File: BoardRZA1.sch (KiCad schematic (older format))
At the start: 183 parts, among them CON1 USB-MINI-B, CON2 USB-A-PCB, CON3 microSD, CON4 BARREL_JACK, J1 HR911105A, J2 SIL38, K1 CONN_3, P1 CONN_5X2, P10 CONN_1, P11 CONN_1, P12 CONN_1, P13 CONN_1, P14 CONN_1, P15 CONN_1, P16 CONN_1, P17 CONN_1, P2 CONN_1, P3 CONN_1, P4 CONN_1, P5 CONN_1, P6 CONN_1, P7 CONN_1, P8 CONN_1, P9 CONN_1, SW1 RESET, SW2 NMI, SW3 SW0, SW4 SW1, U1 RZ-A1L, U2 13MHz, U3 48MHz, U4 N25QXXX, U5 AS4C16M16S, U6 BA3259HFP, U7 BU42xx, U8 KSZ8041MLL, U9 25MHz, X1 32.768k

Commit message: Added VGA out, remove eth
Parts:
- removed C54, C63: 22u, footprints:SM0805, symbol Csmall
- removed C55, C56, C57, C59, C60, C61, C62, C64, C65, C66: 100n, footprints:SM0805, symbol Csmall
- removed C58: 100p, footprints:SM0805, symbol Csmall
- removed J1: HR911105A, footprints:RJ45_Pulse_J403-A, symbol HR911105A
- removed L10: BLM18PG600, footprints:SM0805, symbol INDUCTOR_SMALL
- removed R27, R28, R29, R30, R31, R32: 33R, footprints:SM0805, symbol R
- removed R33, R34, R35: 4K7, footprints:SM0805, symbol R
- removed R36, R37, R49: 220R, footprints:SM0805, symbol R
- removed R38, R39, R40, R41: 49.9, footprints:SM0805, symbol R
- removed U8: KSZ8041MLL, footprints:LQFP48-M05, symbol KSZ8041MLL
- removed U9: 25MHz, footprints:OSC_4PIN, symbol OSC_4PIN
- added J1: VGA, footprints:DB_15F-VGA, symbol VGA
- added RP1, RP2, RP3: 20k, Resistors_SMD:r_cat16-8, symbol R_PACK8
- added RP4, RP5, RP6: 10k, Resistors_SMD:r_cat16-8, symbol R_PACK8
- added U8: TL074, SMD_Packages:SO14E, symbol TL074
- R21: value 6.49k -> 10k
- R22: value 4K7 -> 10k
- R23: value 33R -> 10k
- R24, R25, R26: value 33R -> 280R
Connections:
- net ET_MDC is gone; now on net LED2: U1.72 (P9_0/ET_MDC/SD_D1_0/TxD1)
- net ET_MDIO is gone; now on net LED3: U1.73 (P9_1/ET_MDIO/SD_D0_0/CTS0)
- net PHY_RESET is gone; now on net SW1: U1.189 (P4_1/A18/VIO_HD/TIOC2B/ET_MDIO/RTS1)
- net +3.3V: now also U8.4 (V+); no longer R22.1
- net LED0: now also U1.70 (P8_14/LCD0_TCON6/ET_COL/SD_CD_0/SCK1); no longer U1.17 (P6_0/D16/LCD0_DATA8/RSPCK0/TCLKA/WDTOVF)
- net LED1: now also U1.71 (P8_15/ET_CRS/SD_WP_0/RxD1); no longer U1.19 (P6_1/D17/LCD0_DATA9/SSL00/TCLKB)
- net LED2: no longer U1.20 (P6_2/D18/LCD0_DATA10/MOSI0/TCLKC)
- net LED3: no longer U1.22 (P6_3/D19/LCD0_DATA11/MISO0/TCLKD)
- net P1_10: now also J2.23; no longer J2.19
- net P1_11: now also J2.22; no longer J2.18
- net P1_12: now also J2.21; no longer J2.17
- net P1_13: now also J2.20; no longer J2.16
- net P1_14: now also J2.19; no longer J2.15
- net P1_15: now also J2.18; no longer J2.14
- net P1_8: now also J2.25; no longer J2.21
- net P1_9: now also J2.24; no longer J2.20
- net P7_10: now also J2.29; no longer J2.25
- net P7_11: now also J2.28; no longer J2.24
- net P7_8: now also J2.31; no longer J2.27
- net P7_9: now also J2.30; no longer J2.26
- net P8_12: now also J2.27; no longer J2.23
- net P8_13: now also J2.26; no longer J2.22
- net SW0: now also U1.188 (P4_0/A17/VIO_VD/TIOC1B/ET_MDC/CTS1); no longer U1.26 (P6_5/D21/LCD0_DATA13/SSIWS3/MLB_SIG)
- net SW1: no longer U1.24 (P6_4/D20/LCD0_DATA12/SSISCK3/MLB_CLK)
- net VSS: now also R22.1, R23.1, J1.10 (GND_VSYNC), J1.5 (GND_HSYNC), J1.6 (RED_RTN), J1.7 (GREEN_RTN), J1.8 (BLUE_RTN), J1.9 (KEY/PWR), U8.11 (V-)
- net P9_5: now reaches U1.137 (P9_5/MISO2/SD_D2_0/TxD0/TIOC2B)
- net P9_5: now also J2.14
- net at R21.2: now also RP4.9 (R8)
- net at R26.2: now also J1.1 (RED)
- net at R22.2: now also RP5.9 (R8)
- net at R25.2: now also J1.2 (GREEN)
- net at R24.2: now also J1.3 (BLUE)
- net at R23.2: now also RP6.9 (R8)
- net ET_COL: no longer names the net of R24.1
- net ET_COL: now also U8.1, U8.2 (-); no longer U1.70 (P8_14/LCD0_TCON6/ET_COL/SD_CD_0/SCK1)
- removed net ET_CRS: R23.1, U1.71 (P8_15/ET_CRS/SD_WP_0/RxD1)
- net ET_RXCLK: no longer names the net of R26.1
- net ET_RXCLK: now also U8.8, U8.9 (-); no longer U1.127 (P9_2/RSPCK2/ET_RXCLK/SD_CLK_0/RTS0/TIOC1A)
- net ET_RXD0 renamed LCD_DATA7
- net LCD_DATA7: now also RP3.1 (P1)
- net ET_RXD1 renamed LCD_HSYNC
- net LCD_HSYNC: now also J1.13 (HSYNC)
- net ET_RXD2 renamed LCD_VSYNC
- net LCD_VSYNC: now also J1.14 (VSYNC)
- net ET_RXD3 renamed LCD_PCLK
- net ET_RXDV renamed P9_4
- net P9_4: now also J2.15
- net ET_RXER renamed P9_3
- net P9_3: now also J2.16
- net ET_TXCLK: no longer names the net of R25.1
- net ET_TXCLK: now also U8.6 (-), U8.7; no longer U1.200 (P8_4/LCD0_DATA4/ET_TXCLK/CTS2/TIOC0A)
- net ET_TXD0 renamed LCD_DATA0
- net LCD_DATA0: now also RP3.8 (P8)
- net ET_TXD1 renamed LCD_DATA1
- net LCD_DATA1: now also RP3.7 (P7)
- net ET_TXD2 renamed LCD_DATA2
- net LCD_DATA2: now also RP3.6 (P6)
- net ET_TXD3 renamed LCD_DATA3
- net LCD_DATA3: now also RP3.5 (P5)
- net ET_TXEN renamed LCD_DATA6
- net LCD_DATA6: now also RP3.2 (P2)
- net P6_10: no longer names the net of J2.33
- net P6_10: no longer U1.40 (P6_10/D26/LCD0_DATA18/SSITxD0/IRQ3/TIOC3D/CAN1_TX)
- net P6_11: no longer names the net of J2.32
- net P6_11: no longer U1.41 (P6_11/D27/LCD0_DATA19/SSIRxD0/SSI_DATA2/SCK0/CAN1_RX)
- net P6_12 renamed LCD_DATA20
- net LCD_DATA20: now also RP1.4 (P4); no longer J2.31
- net P6_13 renamed LCD_DATA21
- net LCD_DATA21: now also RP1.3 (P3); no longer J2.30
- net P6_14 renamed LCD_DATA22
- net LCD_DATA22: now also RP1.2 (P2); no longer J2.29
- net P6_15 renamed LCD_DATA23
- net LCD_DATA23: now also RP1.1 (P1); no longer J2.28
- net P6_6: no longer names the net of J2.37
- net P6_6: no longer U1.31 (P6_6/D22/LCD0_DATA14/SSITxD3/MLB_DAT)
- net P6_7: no longer names the net of J2.36
- net P6_7: no longer U1.32 (P6_7/D23/LCD0_DATA15/SSIRxD3/IRQ0/TIOC3A/RLIN30/RX)
- net P6_8: no longer names the net of J2.35
- net P6_8: no longer U1.33 (P6_8/D24/LCD0_DATA16/SSISCK0/IRQ1/TIOC3B/RLIN30/TX)
- net P6_9: no longer names the net of J2.34
- net P6_9: no longer U1.38 (P6_9/D25/LCD0_DATA17/SSIWS0/IRQ2/TIOC3C)
- net P8_11: no longer names the net of U1.37 (P8_11/LCD0_TCON3/SSISCK2/SCK4)
- net TX_TXER renamed LCD_DATA5
- net LCD_DATA5: now also RP3.3 (P3)
- new net: RP3.9 (R8), RP6.10 (R7), RP6.8 (P8)
- new net: RP3.10 (R7), RP6.11 (R6), RP6.7 (P7)
- new net: RP3.11 (R6), RP6.12 (R5), RP6.6 (P6)
- new net: RP3.12 (R5), RP6.13 (R4), RP6.5 (P5)
- new net: RP3.13 (R4), RP6.14 (R3), RP6.4 (P4)
- new net: RP3.14 (R3), RP6.15 (R2), RP6.3 (P3)
- new net: RP3.15 (R2), RP6.16 (R1), RP6.2 (P2)
- new net: RP2.9 (R8), RP5.10 (R7), RP5.8 (P8)
- new net: RP2.10 (R7), RP5.11 (R6), RP5.7 (P7)
- new net: RP2.11 (R6), RP5.12 (R5), RP5.6 (P6)
- new net: RP2.12 (R5), RP5.13 (R4), RP5.5 (P5)
- new net: RP2.13 (R4), RP5.14 (R3), RP5.4 (P4)
- new net: RP2.14 (R3), RP5.15 (R2), RP5.3 (P3)
- new net: RP2.15 (R2), RP5.16 (R1), RP5.2 (P2)
- new net: RP1.9 (R8), RP4.10 (R7), RP4.8 (P8)
- new net: RP1.10 (R7), RP4.11 (R6), RP4.7 (P7)
- new net: RP1.11 (R6), RP4.12 (R5), RP4.6 (P6)
- new net: RP1.12 (R5), RP4.13 (R4), RP4.5 (P5)
- new net: RP1.13 (R4), RP4.14 (R3), RP4.4 (P4)
- new net: RP1.14 (R3), RP4.15 (R2), RP4.3 (P3)
- new net: RP1.15 (R2), RP4.16 (R1), RP4.2 (P2)
- new net LCD_DATA10: RP2.6 (P6), U1.20 (P6_2/D18/LCD0_DATA10/MOSI0/TCLKC)
- new net LCD_DATA11: RP2.5 (P5), U1.22 (P6_3/D19/LCD0_DATA11/MISO0/TCLKD)
- new net LCD_DATA12: RP2.4 (P4), U1.24 (P6_4/D20/LCD0_DATA12/SSISCK3/MLB_CLK)
- new net LCD_DATA13: RP2.3 (P3), U1.26 (P6_5/D21/LCD0_DATA13/SSIWS3/MLB_SIG)
- new net LCD_DATA14: RP2.2 (P2), U1.31 (P6_6/D22/LCD0_DATA14/SSITxD3/MLB_DAT)
- new net LCD_DATA15: RP2.1 (P1), U1.32 (P6_7/D23/LCD0_DATA15/SSIRxD3/IRQ0/TIOC3A/RLIN30/RX)
- new net LCD_DATA16: RP1.8 (P8), U1.33 (P6_8/D24/LCD0_DATA16/SSISCK0/IRQ1/TIOC3B/RLIN30/TX)
- new net LCD_DATA17: RP1.7 (P7), U1.38 (P6_9/D25/LCD0_DATA17/SSIWS0/IRQ2/TIOC3C)
- new net LCD_DATA18: RP1.6 (P6), U1.40 (P6_10/D26/LCD0_DATA18/SSITxD0/IRQ3/TIOC3D/CAN1_TX)
- new net LCD_DATA19: RP1.5 (P5), U1.41 (P6_11/D27/LCD0_DATA19/SSIRxD0/SSI_DATA2/SCK0/CAN1_RX)
- new net LCD_DATA4: RP3.4 (P4), U1.200 (P8_4/LCD0_DATA4/ET_TXCLK/CTS2/TIOC0A)
- new net LCD_DATA8: RP2.8 (P8), U1.17 (P6_0/D16/LCD0_DATA8/RSPCK0/TCLKA/WDTOVF)
- new net LCD_DATA9: RP2.7 (P7), U1.19 (P6_1/D17/LCD0_DATA9/SSL00/TCLKB)
- new net P9_2: J2.17, U1.127 (P9_2/RSPCK2/ET_RXCLK/SD_CLK_0/RTS0/TIOC1A)
- new net VGA_B: RP1.16 (R1), RP4.1 (P1), U8.3 (+)
- new net VGA_G: RP2.16 (R1), RP5.1 (P1), U8.5 (+)
- new net VGA_R: RP3.16 (R1), RP6.1 (P1), U8.10 (+)
- no-connect marks 17 -> 14
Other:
- note removed: "LED0: PU\nLED1: PD"

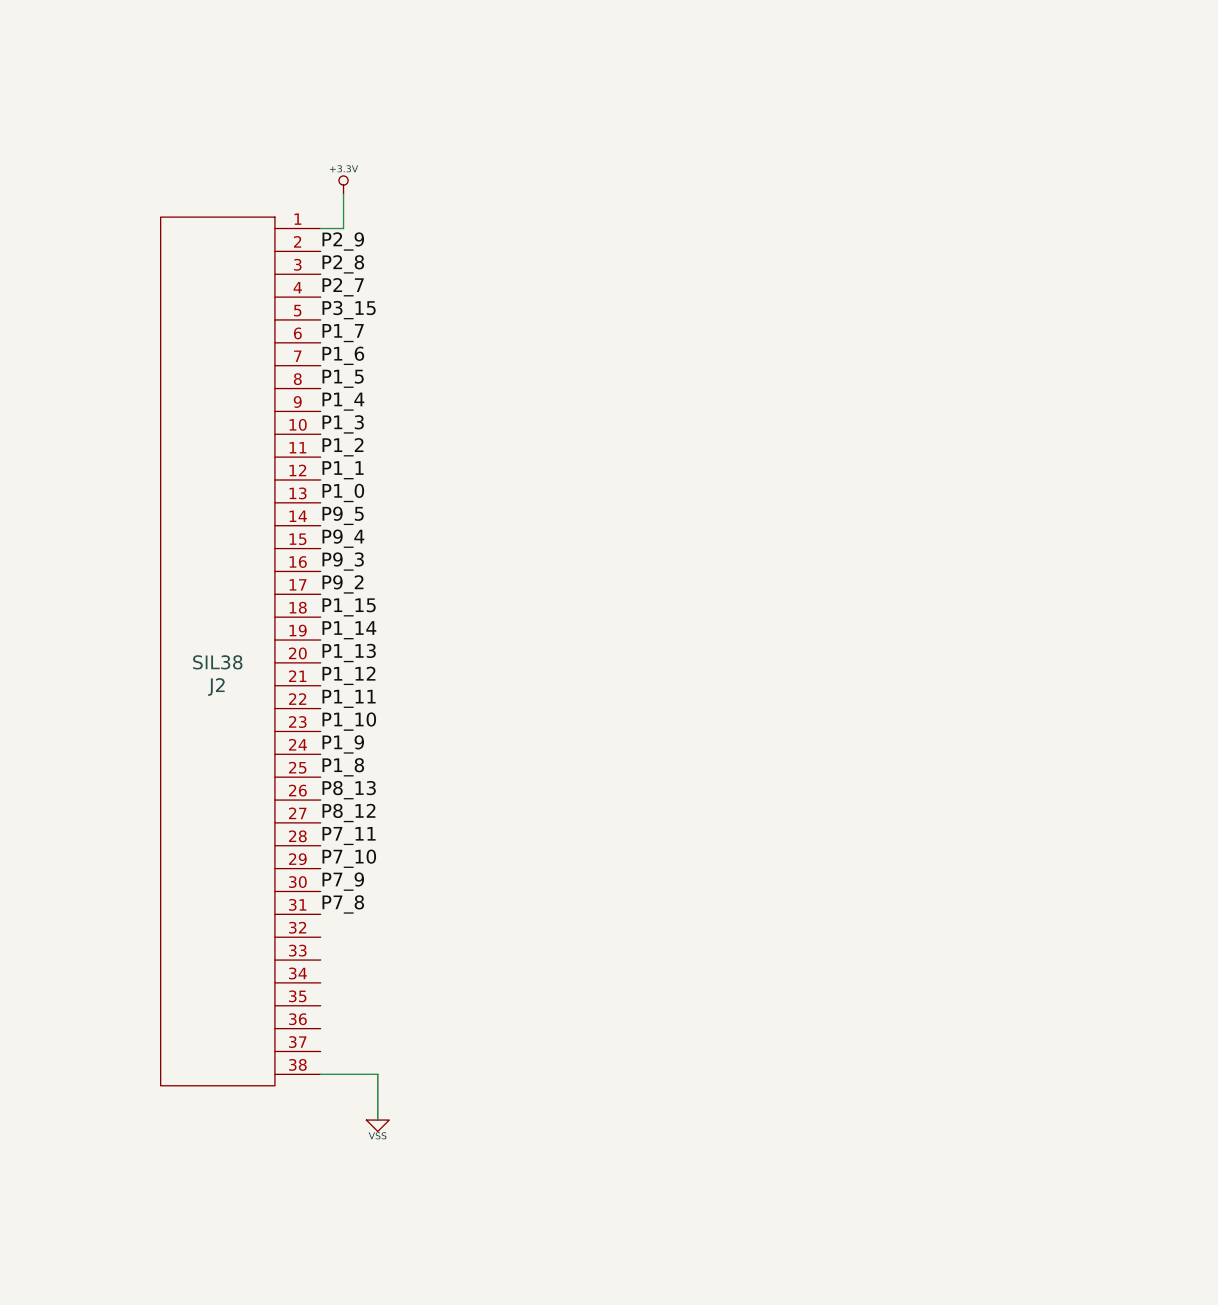
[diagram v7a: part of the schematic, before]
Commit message: Resize board, move VGA connector and R2R DAC
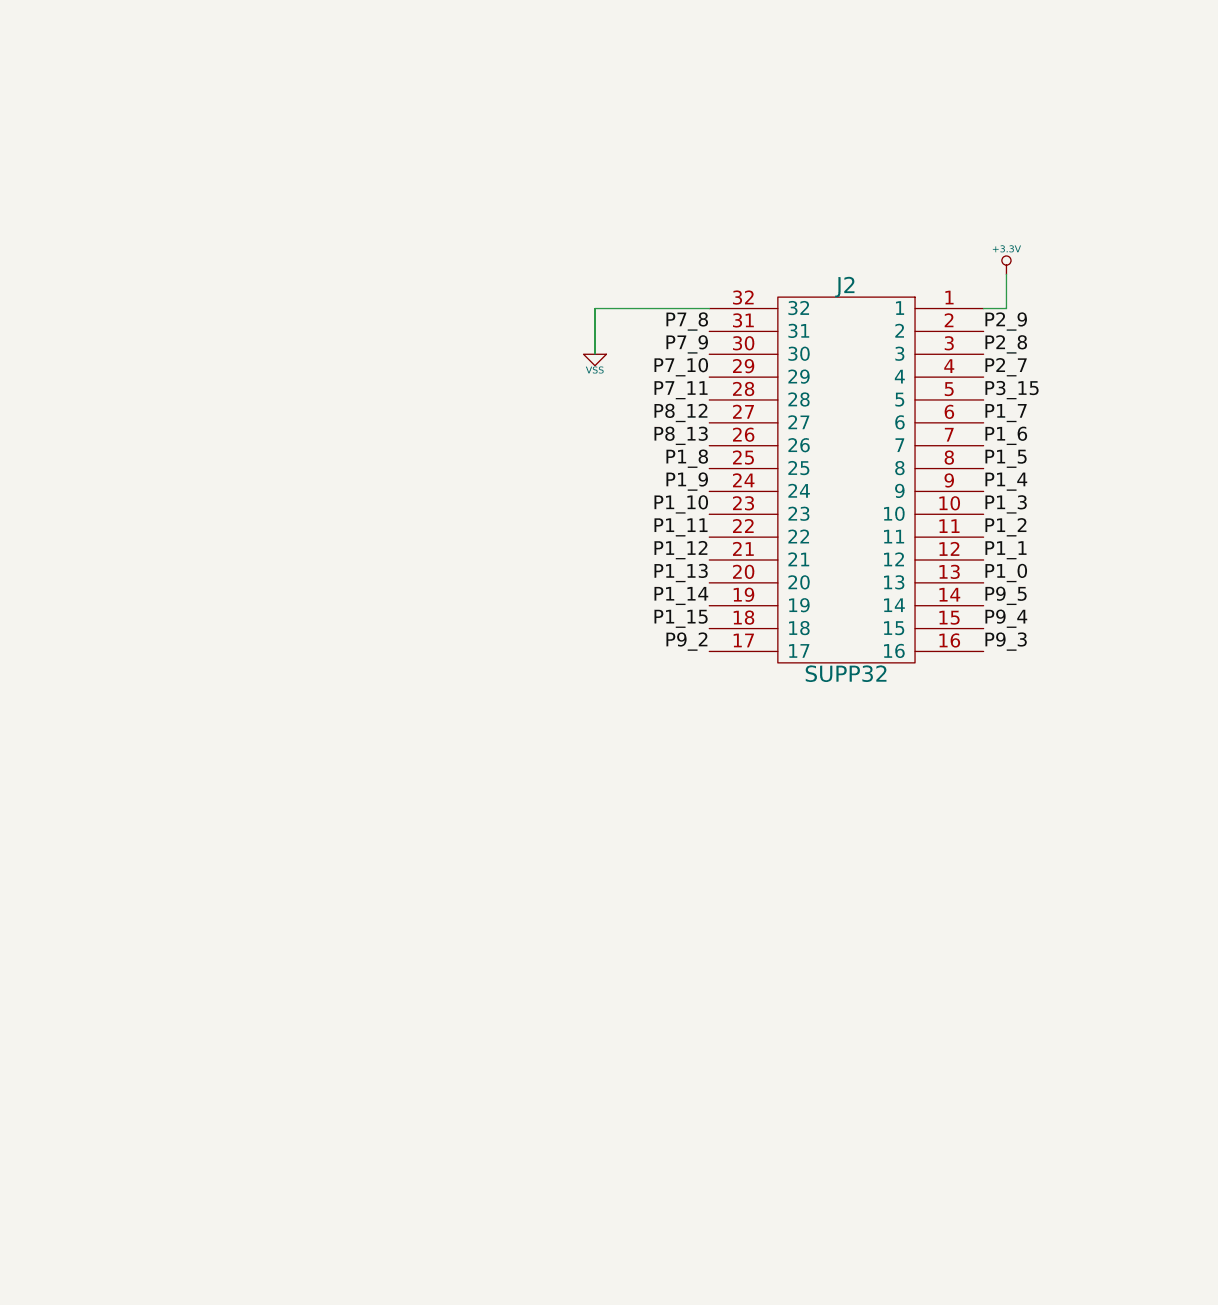
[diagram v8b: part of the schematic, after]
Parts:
- removed J2: SIL38, footprints:Pin_Header_Angled_1x38, symbol SIL38
- added J2: SUPP32, Pin_Headers:Pin_Header_Angled_1x32, symbol SUPP32
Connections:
- net +3.3V: now also J2.1
- net P1_0: now also J2.13
- net P1_1: now also J2.12
- net P1_10: now also J2.23
- net P1_11: now also J2.22
- net P1_12: now also J2.21
- net P1_13: now also J2.20
- net P1_14: now also J2.19
- net P1_15: now also J2.18
- net P1_2: now also J2.11
- net P1_3: now also J2.10
- net P1_4: now also J2.9
- net P1_5: now also J2.8
- net P1_6: now also J2.7
- net P1_7: now also J2.6
- net P1_8: now also J2.25
- net P1_9: now also J2.24
- net P2_7: now also J2.4
- net P2_8: now also J2.3
- net P2_9: now also J2.2
- net P3_15: now also J2.5
- net P7_10: now also J2.29
- net P7_11: now also J2.28
- net P7_8: now also J2.31
- net P7_9: now also J2.30
- net P8_12: now also J2.27
- net P8_13: now also J2.26
- net P9_2: now also J2.17
- net P9_3: now also J2.16
- net P9_4: now also J2.15
- net P9_5: now also J2.14
- net VSS: now also J2.32
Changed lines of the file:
@@
 L VSS #PWR048
 U 1 1 546806AB
-P 8350 12150
-F 0 "#PWR048" H 8350 12150 30  0001 C CNN
-F 1 "VSS" H 8350 12080 30  0000 C CNN
-F 2 "" H 8350 12150 60  0000 C CNN
-F 3 "" H 8350 12150 60  0000 C CNN
-	1    8350 12150
-	1    0    0    -1
+P 9300 8800
+F 0 "#PWR048" H 9300 8800 30  0001 C CNN
+F 1 "VSS" H 9300 8730 30  0000 C CNN
+F 2 "" H 9300 8800 60  0000 C CNN
+F 3 "" H 9300 8800 60  0000 C CNN
+	1    9300 8800
+	-1   0    0    -1
 $EndComp
 $Comp
 L +3.3V #PWR049
 U 1 1 54681794
-P 8200 8100
-F 0 "#PWR049" H 8200 8060 30  0001 C CNN
-F 1 "+3.3V" H 8200 8210 30  0000 C CNN
-F 2 "" H 8200 8100 60  0000 C CNN
-F 3 "" H 8200 8100 60  0000 C CNN
-	1    8200 8100
-	1    0    0    -1
-$EndComp
-$Comp
-L SIL38 J2
-U 1 1 5468523A
-P 7650 10200
-F 0 "J2" H 7650 10150 60  0000 C CNN
-F 1 "SIL38" H 7650 10250 60  0000 C CNN
-F 2 "footprints:Pin_Header_Angled_1x38" H 7650 10200 60  0001 C CNN
-F 3 "" H 7650 10200 60  0000 C CNN
-	1    7650 10200
-	-1   0    0    -1
+P 11100 8450
+F 0 "#PWR049" H 11100 8410 30  0001 C CNN
+F 1 "+3.3V" H 11100 8560 30  0000 C CNN
+F 2 "" H 11100 8450 60  0000 C CNN
+F 3 "" H 11100 8450 60  0000 C CNN
+	1    11100 8450
+	1    0    0    -1
 $EndComp
 Text Label 27950 13350 0    60   ~ 0
@@
 Text Label 27950 12650 0    60   ~ 0
 P1_7
-Text Label 8100 9450 0    60   ~ 0
+Text Label 11000 9800 0    60   ~ 0
 P1_0
-Text Label 8100 9350 0    60   ~ 0
+Text Label 11000 9700 0    60   ~ 0
 P1_1
-Text Label 8100 9250 0    60   ~ 0
+Text Label 11000 9600 0    60   ~ 0
 P1_2
-Text Label 8100 9150 0    60   ~ 0
+Text Label 11000 9500 0    60   ~ 0
 P1_3
-Text Label 8100 9050 0    60   ~ 0
+Text Label 11000 9400 0    60   ~ 0
 P1_4
-Text Label 8100 8950 0    60   ~ 0
+Text Label 11000 9300 0    60   ~ 0
 P1_5
-Text Label 8100 8850 0    60   ~ 0
+Text Label 11000 9200 0    60   ~ 0
 P1_6
-Text Label 8100 8750 0    60   ~ 0
+Text Label 11000 9100 0    60   ~ 0
 P1_7
 Text Label 27950 12550 0    60   ~ 0
@@
 P2_9
 NoConn ~ 27950 11850
-Text Label 8100 8550 0    60   ~ 0
+Text Label 11000 8900 0    60   ~ 0
 P2_7
-Text Label 8100 8450 0    60   ~ 0
+Text Label 11000 8800 0    60   ~ 0
 P2_8
-Text Label 8100 8350 0    60   ~ 0
+Text Label 11000 8700 0    60   ~ 0
 P2_9
-Text Label 8100 8650 0    60   ~ 0
+Text Label 11000 9000 0    60   ~ 0
 P3_15
 Text Label 18650 17450 2    60   ~ 0
@@
 Text Label 18650 16750 2    60   ~ 0
 P1_8
-Text Label 8100 9950 0    60   ~ 0
+Text Label 9800 10000 2    60   ~ 0
 P1_15
-Text Label 8100 10050 0    60   ~ 0
+Text Label 9800 9900 2    60   ~ 0
 P1_14
-Text Label 8100 10150 0    60   ~ 0
+Text Label 9800 9800 2    60   ~ 0
 P1_13
-Text Label 8100 10250 0    60   ~ 0
+Text Label 9800 9700 2    60   ~ 0
 P1_12
-Text Label 8100 10350 0    60   ~ 0
+Text Label 9800 9600 2    60   ~ 0
 P1_11
-Text Label 8100 10450 0    60   ~ 0
+Text Label 9800 9500 2    60   ~ 0
 P1_10
-Text Label 8100 10550 0    60   ~ 0
+Text Label 9800 9400 2    60   ~ 0
 P1_9
-Text Label 8100 10650 0    60   ~ 0
+Text Label 9800 9300 2    60   ~ 0
 P1_8
 $Comp
@@
 Text Label 18650 14550 2    60   ~ 0
 P8_13
-Text Label 8100 11250 0    60   ~ 0
+Text Label 9800 8700 2    60   ~ 0
 P7_8
-Text Label 8100 11150 0    60   ~ 0
+Text Label 9800 8800 2    60   ~ 0
 P7_9
-Text Label 8100 11050 0    60   ~ 0
+Text Label 9800 8900 2    60   ~ 0
 P7_10
-Text Label 8100 10950 0    60   ~ 0
+Text Label 9800 9000 2    60   ~ 0
 P7_11
 Text Label 18650 14850 2    60   ~ 0
@@
 Text Label 28000 17450 0    60   ~ 0
 MD_BOOT0
-Text Label 8100 10850 0    60   ~ 0
+Text Label 9800 9100 2    60   ~ 0
 P8_12
-Text Label 8100 10750 0    60   ~ 0
+Text Label 9800 9200 2    60   ~ 0
 P8_13
 Text Label 16700 14050 2    60   ~ 0
@@
 Connection ~ 16800 3900
 Wire Wire Line
-	8350 12150 8350 11950
-Wire Wire Line
-	8350 11950 8100 11950
-Wire Wire Line
-	8200 8100 8200 8250
-Wire Wire Line
-	8200 8250 8100 8250
+	9300 8800 9300 8600
+Wire Wire Line
+	9300 8600 9800 8600
+Wire Wire Line
+	11100 8450 11100 8600
+Wire Wire Line
+	11100 8600 11000 8600
 Wire Wire Line
 	15250 3050 15350 3050
@@
 Text Label 27950 14150 0    60   ~ 0
 P9_5
-Text Label 8100 9850 0    60   ~ 0
+Text Label 9800 10100 2    60   ~ 0
 P9_2
-Text Label 8100 9750 0    60   ~ 0
+Text Label 11000 10100 0    60   ~ 0
 P9_3
-Text Label 8100 9650 0    60   ~ 0
+Text Label 11000 10000 0    60   ~ 0
 P9_4
-Text Label 8100 9550 0    60   ~ 0
+Text Label 11000 9900 0    60   ~ 0
 P9_5
+$Comp
+L SUPP32 J2
+U 1 1 54F544B6
+P 10400 9350
+F 0 "J2" H 10400 10200 70  0000 C CNN
+F 1 "SUPP32" H 10400 8500 70  0000 C CNN
+F 2 "Pin_Headers:Pin_Header_Angled_1x32" H 10400 9350 60  0001 C CNN
+F 3 "" H 10400 9350 60  0000 C CNN
+	1    10400 9350
+	-1   0    0    -1
+$EndComp
 $EndSCHEMATC
